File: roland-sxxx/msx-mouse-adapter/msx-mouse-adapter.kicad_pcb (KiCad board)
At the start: 2 copper layers, 51.4 x 32 mm, 14 parts, among them J1 MSX DSUB9 Female, J2 PS/2 USB Connector, J3 PROG, U1 ATmega168PA-AU, Y1 16.000Mhz

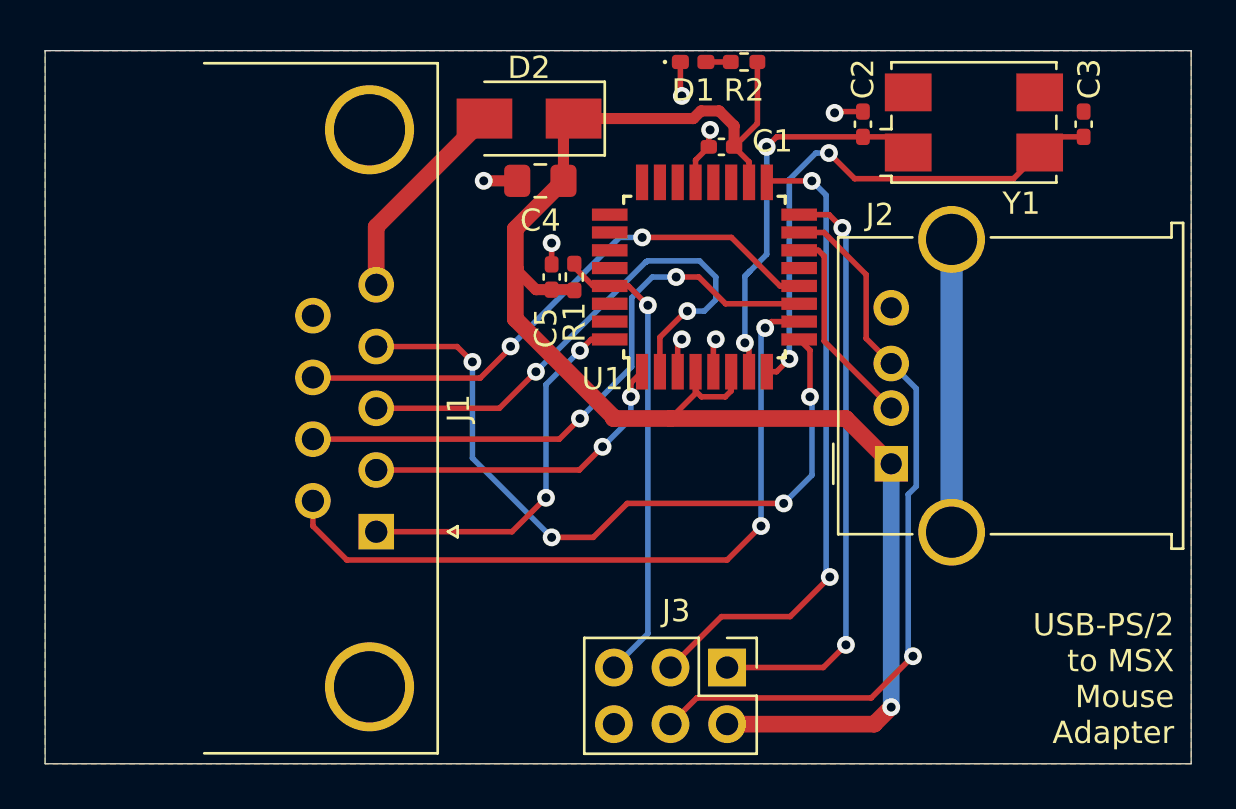
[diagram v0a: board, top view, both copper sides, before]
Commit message: made the mouse adapter more compact.
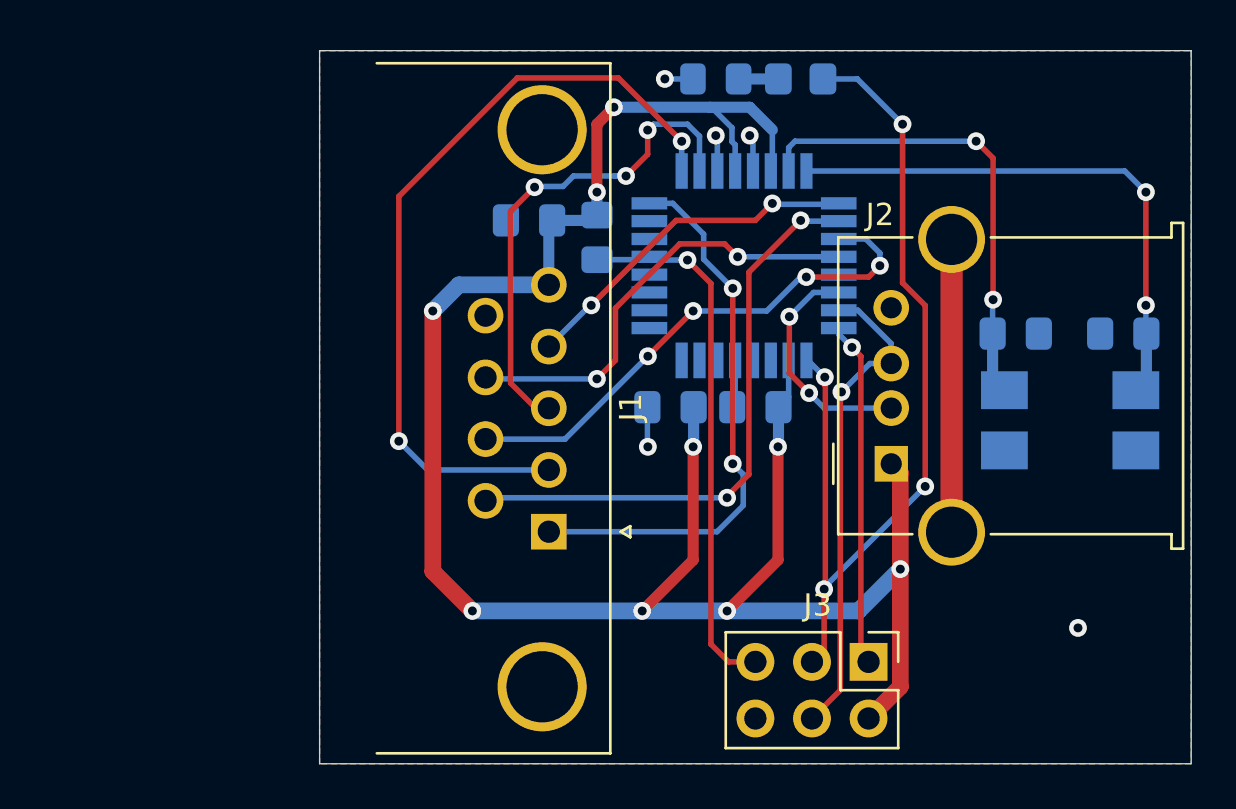
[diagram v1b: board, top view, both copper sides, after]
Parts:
- removed D2: SMA 40V (1N5819), Diode_SMD:D_SMA
- C1, C2, C3, C5: footprint Capacitor_SMD:C_0402_1005Metric_Pad0.74x0.62mm_HandSolder -> Capacitor_SMD:C_0805_2012Metric_Pad1.18x1.45mm_HandSolder; moved to B.Cu
- C4, U1, Y1: moved to B.Cu
- D1: footprint LED_SMD:LED_0402_1005Metric_Pad0.77x0.64mm_HandSolder -> LED_SMD:LED_0805_2012Metric_Pad1.15x1.40mm_HandSolder; moved to B.Cu
- J1: footprint Connector_Dsub:DSUB-9_Female_Horizontal_P2.77x2.84mm_EdgePinOffset4.94mm_Housed_MountingHolesOffset7.48mm -> custom:MSX DSUB9 Female
- R1, R2: footprint Resistor_SMD:R_0402_1005Metric_Pad0.72x0.64mm_HandSolder -> Resistor_SMD:R_0805_2012Metric_Pad1.20x1.40mm_HandSolder; moved to B.Cu
- moved Y1 14.0 mm to (152.3, 50.9)
- moved C1 11.8 mm to (138.2, 50.3)
- moved C4 11.7 mm to (134.4, 50.3)
- moved C2 11.6 mm to (149.9, 47.0), turned to 0 degrees
- moved J1 10.5 mm to (112.3, 50.3)
- moved C3 9.56 mm to (154.7, 47.0), turned to 180 degrees
- moved J3 6.36 mm to (143.3, 61.7)
- moved C5 2.74 mm to (128.0, 41.9), turned to 180 degrees
- moved R2 2.65 mm to (140.2, 35.6)
- moved R1 2.05 mm to (131.1, 42.7), turned to 270 degrees
- moved U1 1.85 mm to (137.7, 43.9), turned to 270 degrees
- moved D1 1.27 mm to (136.4, 35.6)
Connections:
- J1 pad 5: Net-(D2-Pad2) -> +5V
- R2 pad 2: +5V -> /D13_SCK
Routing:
- net +5V: track 72.2 -> 97.6 mm, vias 1 -> 9
- net /D3_PWM: track 14.7 -> 35.7 mm
- net /D5_PWM: track 33.1 -> 15.7 mm, vias 4 -> 2
- net /D13_SCK: track 29.0 -> 42.0 mm, vias 2 -> 4
- net /D11_MOSI: track 34.2 -> 21.8 mm
- net /D12_MISO: track 26.7 -> 15.5 mm, vias 2 -> 1
- net Net-(D2-Pad2): track 9.47 -> 0.00 mm
- net /D2: track 17.1 -> 25.1 mm
- net /ButtonLeft: track 33.1 -> 26.4 mm
- net /D8: track 25.4 -> 20.0 mm
- net Net-(C2-Pad1): track 17.8 -> 21.3 mm
- net /ButtonRight: track 27.2 -> 23.8 mm, vias 2 -> 4
- net /RESET: track 21.1 -> 24.2 mm
- net GND: track 11.0 -> 8.48 mm, vias 7 -> 5
- net /D4: track 24.0 -> 22.4 mm, vias 2 -> 3
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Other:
- board size 51.4 x 32 mm -> 39.1 x 32 mm
- board text removed: "USB-PS/2 to MSX Mouse Adapter"
